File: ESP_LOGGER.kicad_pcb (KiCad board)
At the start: 2 copper layers, 25 parts, among them SW1 SW_Push, SW2 SW_Push, U1 AZ1086_SOT223

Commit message: pcb F.Cu
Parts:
- removed BATTERY1: Conn_01x02_Female, Connectors_Molex:Molex_PicoBlade_53047-0210_02x1.25mm_Straight
- removed ESP_I2C1, ESP_PWR1: Conn_01x02_Female, Pin_Headers:Pin_Header_Straight_1x02_Pitch2.54mm
- removed ESP_LED1: Conn_01x01_Female, Pin_Headers:Pin_Header_Straight_1x01_Pitch2.54mm
- removed ESP_SD1: Conn_01x05_Female, Pin_Headers:Pin_Header_Straight_1x05_Pitch2.54mm
- removed FTDI1: Conn_01x05_Male, Pin_Headers:Pin_Header_Straight_1x05_Pitch2.54mm
- added ESP_COM1: Conn_01x08_Female, Connector_PinSocket_2.54mm:PinSocket_1x08_P2.54mm_Vertical, F.Cu at (151.1, 55.9)
- added ESP_VDD1: Conn_01x02_Female, Connector_PinSocket_2.54mm:PinSocket_1x02_P2.54mm_Vertical, F.Cu at (119.4, 55.9)
- added JBATT1: Conn_01x02_Female, Connector_Molex:Molex_PicoBlade_53047-0410_1x02_P1.25mm_Vertical, F.Cu at (119.4, 83.8)
- added JFTDI1: Conn_01x05_Female, Connector_PinSocket_2.54mm:PinSocket_1x05_P2.54mm_Vertical, F.Cu at (139.7, 83.8)
- added TP1: TestPoint, TestPoint:TestPoint_Loop_D2.54mm_Drill1.5mm_Beaded, F.Cu at (146.1, 73.7)
- added TP2: TestPoint, TestPoint:TestPoint_Loop_D2.54mm_Drill1.5mm_Beaded, F.Cu at (146.1, 68.6)
- added TP3: TestPoint, TestPoint:TestPoint_Loop_D2.54mm_Drill1.5mm_Beaded, F.Cu at (179.1, 58.4)
- added TP4: TestPoint, TestPoint:TestPoint_Loop_D2.54mm_Drill1.5mm_Beaded, F.Cu at (172.7, 80.0)
- added TP5: TestPoint, TestPoint:TestPoint_Loop_D2.54mm_Drill1.5mm_Beaded, F.Cu at (177.8, 53.3)
- added TP7: TestPoint, TestPoint:TestPoint_Loop_D2.54mm_Drill1.5mm_Beaded, F.Cu at (183.5, 43.2)
- C1: value 10uF -> 100u; footprint Capacitors_SMD:C_0805_HandSoldering -> Capacitor_SMD:C_0805_2012Metric_Pad1.15x1.40mm_HandSolder
- C2: value 0.1uF -> 1u; footprint Capacitors_SMD:C_0805_HandSoldering -> Capacitor_SMD:C_0805_2012Metric_Pad1.15x1.40mm_HandSolder
- C3, C4: value 1nF -> 1n; footprint Capacitors_SMD:C_0805_HandSoldering -> Capacitor_SMD:C_0805_2012Metric_Pad1.15x1.40mm_HandSolder
- D1: footprint Diodes_ThroughHole:D_5W_P10.16mm_Horizontal -> Diode_THT:D_A-405_P7.62mm_Horizontal
- D2: footprint Diodes_ThroughHole:D_T-1_P2.54mm_Vertical_AnodeUp -> LED_THT:LED_D5.0mm_Clear
- ESP_SWT1, ESP_UART1: footprint Pin_Headers:Pin_Header_Straight_1x02_Pitch2.54mm -> Connector_PinSocket_2.54mm:PinSocket_1x02_P2.54mm_Vertical
- MICROSD1: footprint Pin_Headers:Pin_Header_Straight_1x08_Pitch2.54mm -> Connector_PinSocket_2.54mm:PinSocket_1x08_P2.54mm_Vertical
- MPU1: footprint Pin_Headers:Pin_Header_Straight_1x04_Pitch2.54mm -> Connector_PinSocket_2.54mm:PinSocket_1x04_P2.54mm_Vertical
- R1, R2, R3: value 10k -> R; footprint Resistors_ThroughHole:R_Axial_DIN0207_L6.3mm_D2.5mm_P10.16mm_Horizontal -> Resistor_THT:R_Axial_DIN0207_L6.3mm_D2.5mm_P10.16mm_Horizontal
- R4, R5, R6: footprint Resistors_ThroughHole:R_Axial_DIN0207_L6.3mm_D2.5mm_P10.16mm_Horizontal -> Resistor_THT:R_Axial_DIN0207_L6.3mm_D2.5mm_P10.16mm_Horizontal
- SW1, SW2: footprint Buttons_Switches_SMD:SW_SPST_EVQPE1 -> Button_Switch_THT:SW_PUSH_6mm
- U1: footprint TO_SOT_Packages_SMD:SOT-223-3_TabPin2 -> Package_TO_SOT_SMD:SOT-223
- moved C4 99.6 mm to (174.0, 48.3), turned to 90 degrees
- moved C3 94.9 mm to (174.0, 53.3), turned to 90 degrees
- moved ESP_UART1 90.6 mm to (137.2, 44.5), turned to 90 degrees
- moved SW2 88.8 mm to (161.4, 41.4), turned to 0 degrees
- moved SW1 83.8 mm to (161.2, 49.5), turned to 0 degrees
- moved R3 76.3 mm to (157.5, 47.0), turned to 180 degrees
- moved R2 73.7 mm to (157.5, 50.8), turned to 180 degrees
- moved R6 70.3 mm to (168.9, 59.7)
- moved R5 70.3 mm to (168.9, 63.5)
- moved R1 62.1 mm to (168.9, 67.3), turned to 180 degrees
- moved U1 57.0 mm to (148.6, 87.6), turned to 90 degrees
- moved MICROSD1 56.2 mm to (179.1, 64.8)
- moved MPU1 56.1 mm to (158.8, 81.3), turned to 0 degrees
- moved R4 55.5 mm to (168.9, 73.7)
- moved D1 54.5 mm to (124.5, 88.9)
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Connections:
- C1 pad 1: VCC -> 3.3V
- C2 pad 1: VCC -> 3.3V
- MICROSD1 pad 1: CD -> J_CD
- MICROSD1 pad 5: CLK -> J_CLK
- R1 pad 1: VCC -> 3.3V
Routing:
- net 3.3V: track 0.00 -> 175.4 mm
- net D3: track 0.00 -> 102.1 mm
- net CMD: track 0.00 -> 90.1 mm
- net D0: track 0.00 -> 52.3 mm
- net PC_TX: track 0.00 -> 39.4 mm
- net PC_RX: track 0.00 -> 39.4 mm
- net S_SCL: track 0.00 -> 33.7 mm
- net PC_5V: track 0.00 -> 27.0 mm
- net BOOT: track 0.00 -> 25.8 mm
- net EN: track 0.00 -> 25.5 mm
- net S_SDA: track 0.00 -> 23.5 mm
- net Net-(C4-Pad2): track 0.00 -> 23.0 mm
- net Net-(C3-Pad2): track 0.00 -> 18.5 mm
- net BATT_GND: track 0.00 -> 16.7 mm, vias 0 -> 2
- net Net-(D2-Pad2): track 0.00 -> 11.7 mm
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- added copper zone on F.Cu, net BATT_GND
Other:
- board outline added: 75.6 x 62.2 mm
- net class Default: trace_width 0.25 -> 0.5

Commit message: bugfix
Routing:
- net IO_LED: track 7.62 -> 15.2 mm
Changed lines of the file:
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@@
     (thickness 1.6)
     (drawings 30)
-    (tracks 160)
+    (tracks 162)
     (zones 0)
     (modules 29)
@@
   (segment (start 153.67 73.66) (end 158.75 73.66) (width 0.5) (layer F.Cu) (net 21) (status 30))
   (segment (start 152.4 73.66) (end 154.94 73.66) (width 0.5) (layer F.Cu) (net 21))
+  (segment (start 151.13 73.66) (end 152.4 73.66) (width 0.5) (layer F.Cu) (net 21))
+  (segment (start 152.4 73.66) (end 158.75 73.66) (width 0.5) (layer F.Cu) (net 21))
   (segment (start 179.07 58.42) (end 179.07 64.77) (width 0.5) (layer F.Cu) (net 22) (status 30))
   (segment (start 177.8 74.93) (end 179.07 74.93) (width 0.5) (layer F.Cu) (net 23) (status 20))

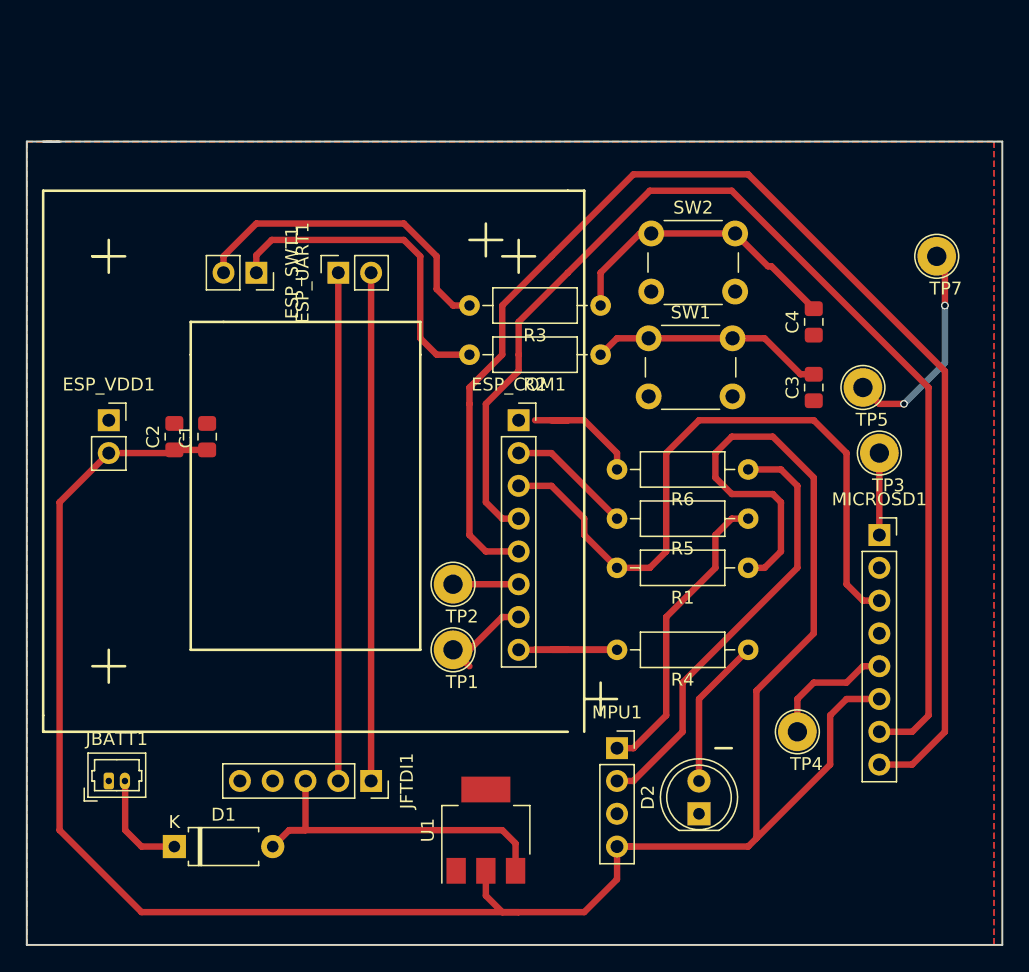
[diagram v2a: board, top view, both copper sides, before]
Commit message: improvement in the size and usability
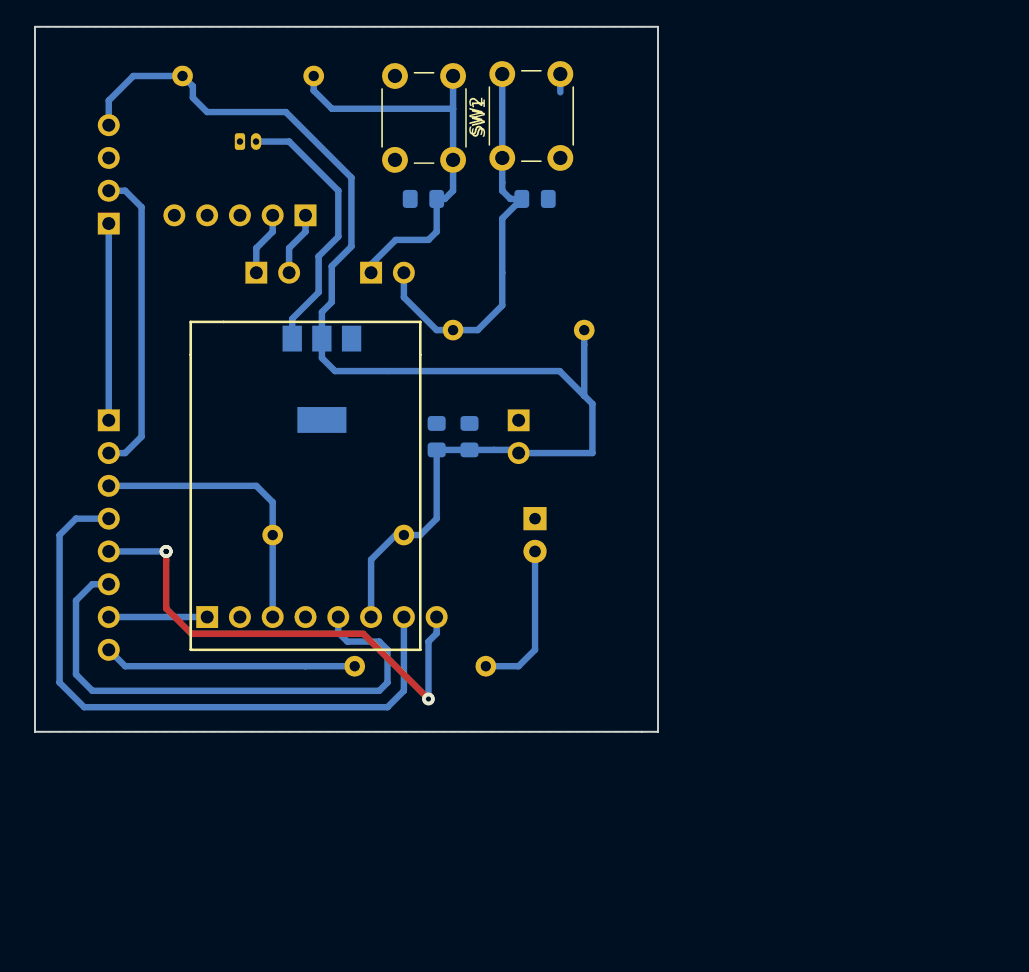
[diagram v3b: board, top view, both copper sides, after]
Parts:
- removed D1: DIODE, Diode_THT:D_A-405_P7.62mm_Horizontal
- removed R5, R6: 10k, Resistor_THT:R_Axial_DIN0207_L6.3mm_D2.5mm_P10.16mm_Horizontal
- removed TP1, TP2, TP3, TP4, TP5, TP7: TestPoint, TestPoint:TestPoint_Loop_D2.54mm_Drill1.5mm_Beaded
- C1, C2, C3, C4, D2, ESP_COM1, ESP_SWT1, ESP_UART1, ESP_VDD1, JBATT1, JFTDI1, MICROSD1, MPU1, R1, R4, U1: moved to B.Cu
- R2, R3: value R -> 10k; moved to B.Cu
- moved MPU1 56.6 mm to (119.4, 40.6)
- moved MICROSD1 52.5 mm to (127.0, 71.1), turned to 270 degrees
- moved JBATT1 50.6 mm to (129.5, 34.3)
- moved JFTDI1 44.1 mm to (134.6, 40.0), turned to 90 degrees
- moved U1 37.2 mm to (135.9, 52.7), turned to 270 degrees
- moved C3 33.6 mm to (143.8, 38.7), turned to 0 degrees
- moved ESP_COM1 31.8 mm to (119.4, 55.9), turned to 180 degrees
- moved ESP_VDD1 31.8 mm to (151.1, 55.9), turned to 180 degrees
- moved R2 31.0 mm to (135.3, 29.2)
- moved R1 26.8 mm to (142.2, 64.8)
- moved D2 26.2 mm to (152.4, 63.5), turned to 270 degrees
- moved SW1 25.3 mm to (146.1, 29.2), turned to 270 degrees
- moved C4 23.6 mm to (152.4, 38.7), turned to 180 degrees
- moved C2 22.9 mm to (147.3, 57.1)
- moved R4 20.4 mm to (148.6, 74.9)
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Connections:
- net CMD renamed DI
- net D3 renamed CS
- C3 pad 2: Net-(C3-Pad2) -> BOOT
- C4 pad 2: Net-(C4-Pad2) -> EN
- ESP_COM1 pad 6: CLK -> SCK
- JFTDI1 pad 3: PC_5V -> (no net)
- MICROSD1 pad 1: J_CD -> CD
- MICROSD1 pad 5: J_CLK -> SCK
- MPU1 pad 1: S_SDA -> SDA
- MPU1 pad 2: S_SCL -> SCL
- R2 pad 1: Net-(C3-Pad2) -> BOOT
- R2 pad 2: BOOT -> 3.3V
- R3 pad 1: Net-(C4-Pad2) -> EN
- R3 pad 2: EN -> 3.3V
- SW1 pad 1: Net-(C3-Pad2) -> BOOT
- SW2 pad 1: Net-(C4-Pad2) -> EN
- U1 pad 1: BATT_GND -> BATT
- U1 pad 3: PC_5V -> BATT_GND
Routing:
- net 3.3V: track 175.4 -> 99.8 mm
- net CS: track 102.1 -> 39.3 mm, vias 0 -> 3
- net SCK: track 0.00 -> 41.8 mm
- net DI: track 90.1 -> 49.5 mm
- net PC_TX: track 39.4 -> 4.97 mm
- net PC_RX: track 39.4 -> 4.97 mm
- net S_SCL: track 33.7 -> 0.00 mm
- net D0: track 52.3 -> 22.1 mm
- net PC_5V: track 27.0 -> 0.00 mm
- net S_SDA: track 23.5 -> 0.00 mm
- net Net-(C4-Pad2): track 23.0 -> 0.00 mm
- net Net-(C3-Pad2): track 18.5 -> 0.00 mm
- net BATT_GND: track 16.7 -> 1.76 mm, vias 2 -> 0
- net SCL: track 9.72 -> 23.9 mm
- net BATT: track 8.15 -> 20.9 mm
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- added copper zone on B.Cu, net BATT_GND
- removed copper zone on F.Cu, net BATT_GND
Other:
- board size 75.6 x 62.2 mm -> 48.3 x 54.6 mm
- net class Default: via_dia 0.6 -> 1
- net class POWER added: clearance 0.2, trace_width 1, via_dia 1, via_drill 0.4
